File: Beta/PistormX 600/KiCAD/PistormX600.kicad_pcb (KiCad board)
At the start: 2 copper layers, 81.9 x 50.8 mm, 27 parts, among them J1 MC68000FN socket, J2 Raspberry_Pi_2_3, J3 PROG, J4 OVR, J5 Power, U1 XC95144XL-TQ100, U2 SPX3819M5-L-3-3, U3 XC6206PxxxMR, U4 CY62177ESL-55ZXI

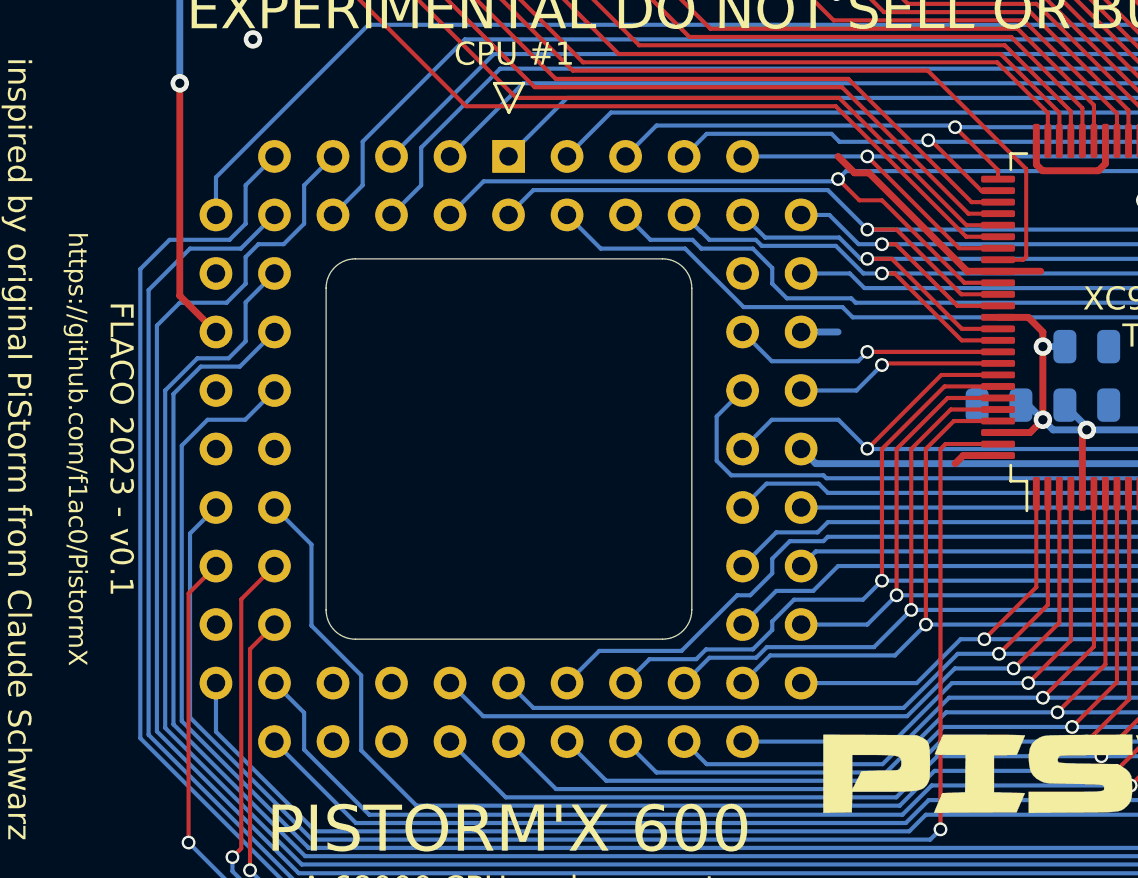
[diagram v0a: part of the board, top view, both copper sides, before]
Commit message: PiStorm'X 500 and PiStorm'X 600 corrections. PiStorm'X 600 is actually working and under test. PiStorm'X 500 will be tested after I find an Agnus 8375 or A500 motherboard replacement.
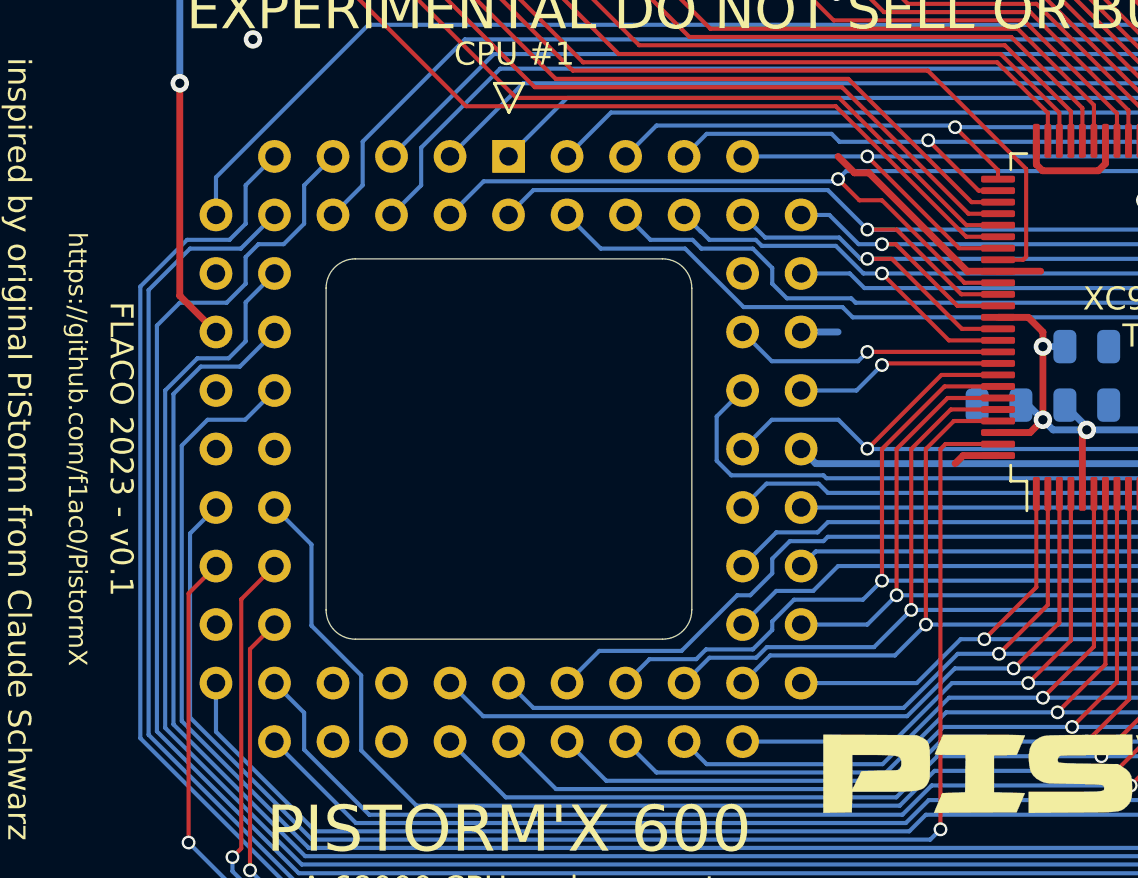
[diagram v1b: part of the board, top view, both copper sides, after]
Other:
- rule pad_to_mask_clearance: 0 -> 0.038
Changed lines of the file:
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@@
       (dielectric_constraints no)
     )
-    (pad_to_mask_clearance 0)
+    (pad_to_mask_clearance 0.038)
+    (solder_mask_min_width 0.1)
     (pcbplotparams
       (layerselection 0x00010fc_ffffffff)
@@
   (segment (start 73.025 136.525) (end 74.422 135.128) (width 0.18) (layer "B.Cu") (net 12))
   (segment (start 74.422 135.128) (end 75.780564 135.128) (width 0.18) (layer "B.Cu") (net 12))
-  (segment (start 108.452096 127.85) (end 109.1775 127.85) (width 0.18) (layer "F.Cu") (net 13))
-  (segment (start 106.266596 125.6645) (end 108.452096 127.85) (width 0.18) (layer "F.Cu") (net 13))
+  (segment (start 108.335395 127.85) (end 109.1775 127.85) (width 0.18) (layer "F.Cu") (net 13))
+  (segment (start 106.149895 125.6645) (end 108.335395 127.85) (width 0.18) (layer "F.Cu") (net 13))
   (segment (start 140.97 125.095) (end 141.45 125.575) (width 0.18) (layer "F.Cu") (net 13))
   (segment (start 141.45 125.575) (end 141.45 128.1075) (width 0.18) (layer "F.Cu") (net 13))
-  (segment (start 106.149895 125.6645) (end 106.266596 125.6645) (width 0.18) (layer "F.Cu") (net 13))
   (via (at 140.97 125.095) (size 0.6) (drill 0.4) (layers "F.Cu" "B.Cu") (net 13))
   (via (at 106.149895 125.6645) (size 0.6) (drill 0.4) (layers "F.Cu" "B.Cu") (net 13))
@@
   (segment (start 106.084395 125.73) (end 102.2985 125.73) (width 0.18) (layer "B.Cu") (net 13))
   (segment (start 106.149895 125.6645) (end 106.215395 125.73) (width 0.18) (layer "B.Cu") (net 13))
-  (segment (start 107.599889 134.35) (end 109.1775 134.35) (width 0.18) (layer "F.Cu") (net 14))
   (segment (start 140.45 131.445) (end 140.45 128.1075) (width 0.18) (layer "F.Cu") (net 14))
-  (segment (start 104.694889 131.445) (end 107.599889 134.35) (width 0.18) (layer "F.Cu") (net 14))
-  (segment (start 104.14 131.445) (end 104.694889 131.445) (width 0.18) (layer "F.Cu") (net 14))
+  (segment (start 107.045 134.35) (end 109.1775 134.35) (width 0.18) (layer "F.Cu") (net 14))
+  (segment (start 104.14 131.445) (end 107.045 134.35) (width 0.18) (layer "F.Cu") (net 14))
   (via (at 104.14 131.445) (size 0.6) (drill 0.4) (layers "F.Cu" "B.Cu") (net 14))
   (via (at 140.45 131.445) (size 0.6) (drill 0.4) (layers "F.Cu" "B.Cu") (net 14))
@@
   (via (at 138.95 154.305) (size 0.6) (drill 0.4) (layers "F.Cu" "B.Cu") (net 45))
   (via (at 121.285 156.21) (size 0.6) (drill 0.4) (layers "F.Cu" "B.Cu") (net 45))
-  (segment (start 121.285 156.21) (end 119.295 158.2) (width 0.18) (layer "B.Cu") (net 45))
   (segment (start 121.285 156.21) (end 122.555 154.94) (width 0.18) (layer "B.Cu") (net 45))
+  (segment (start 119.295 158.2) (end 78.527375 158.2) (width 0.18) (layer "B.Cu") (net 45))
+  (segment (start 76.5175 127.6175) (end 77.77 126.365) (width 0.18) (layer "B.Cu") (net 45))
+  (segment (start 122.555 154.94) (end 123.825 154.94) (width 0.18) (layer "B.Cu") (net 45))
+  (segment (start 71.945 132.015884) (end 73.976384 129.9845) (width 0.18) (layer "B.Cu") (net 45))
+  (segment (start 121.285 156.21) (end 119.295 158.2) (width 0.18) (layer "B.Cu") (net 45))
   (segment (start 75.819 129.9845) (end 76.5175 129.286) (width 0.18) (layer "B.Cu") (net 45))
   (segment (start 78.527375 158.2) (end 71.945 151.617625) (width 0.18) (layer "B.Cu") (net 45))
-  (segment (start 122.555 154.94) (end 123.825 154.94) (width 0.18) (layer "B.Cu") (net 45))
-  (segment (start 76.5175 127.6175) (end 77.77 126.365) (width 0.18) (layer "B.Cu") (net 45))
-  (segment (start 119.295 158.2) (end 78.527375 158.2) (width 0.18) (layer "B.Cu") (net 45))
-  (segment (start 76.5175 129.286) (end 76.5175 127.6175) (width 0.18) (layer "B.Cu") (net 45))
+  (segment (start 71.945 151.617625) (end 71.945 132.015884) (width 0.18) (layer "B.Cu") (net 45))
+  (segment (start 73.976384 129.9845) (end 75.819 129.9845) (width 0.18) (layer "B.Cu") (net 45))
   (segment (start 123.825 154.94) (end 124.46 154.305) (width 0.18) (layer "B.Cu") (net 45))
-  (segment (start 71.945 131.255) (end 73.2155 129.9845) (width 0.18) (layer "B.Cu") (net 45))
-  (segment (start 73.2155 129.9845) (end 75.819 129.9845) (width 0.18) (layer "B.Cu") (net 45))
+  (segment (start 76.5175 129.286) (end 76.5175 127.6175) (width 0.18) (layer "B.Cu") (net 45))
   (segment (start 124.46 154.305) (end 138.95 154.305) (width 0.18) (layer "B.Cu") (net 45))
-  (segment (start 71.945 151.617625) (end 71.945 131.255) (width 0.18) (layer "B.Cu") (net 45))
   (segment (start 110.49 149.225) (end 112.34 147.375) (width 0.18) (layer "F.Cu") (net 46))
   (segment (start 141.5195 149.225) (end 141.45 149.1555) (width 0.18) (layer "F.Cu") (net 46))
@@
     (connect_pads (clearance 0.3175))
     (min_thickness 0.25) (filled_areas_thickness no)
-    (fill yes (thermal_gap 0.3175) (thermal_bridge_width 0.5))
+    (fill yes (thermal_gap 0.3175) (thermal_bridge_width 0.5) (smoothing fillet) (radius 5))
     (polygon
       (pts
